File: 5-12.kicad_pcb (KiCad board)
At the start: 2 copper layers, 266.7 x 95.2 mm, 136 parts, among them SW1 SW_Push, U1 ATmega32U4-AU, Y1 16MHz

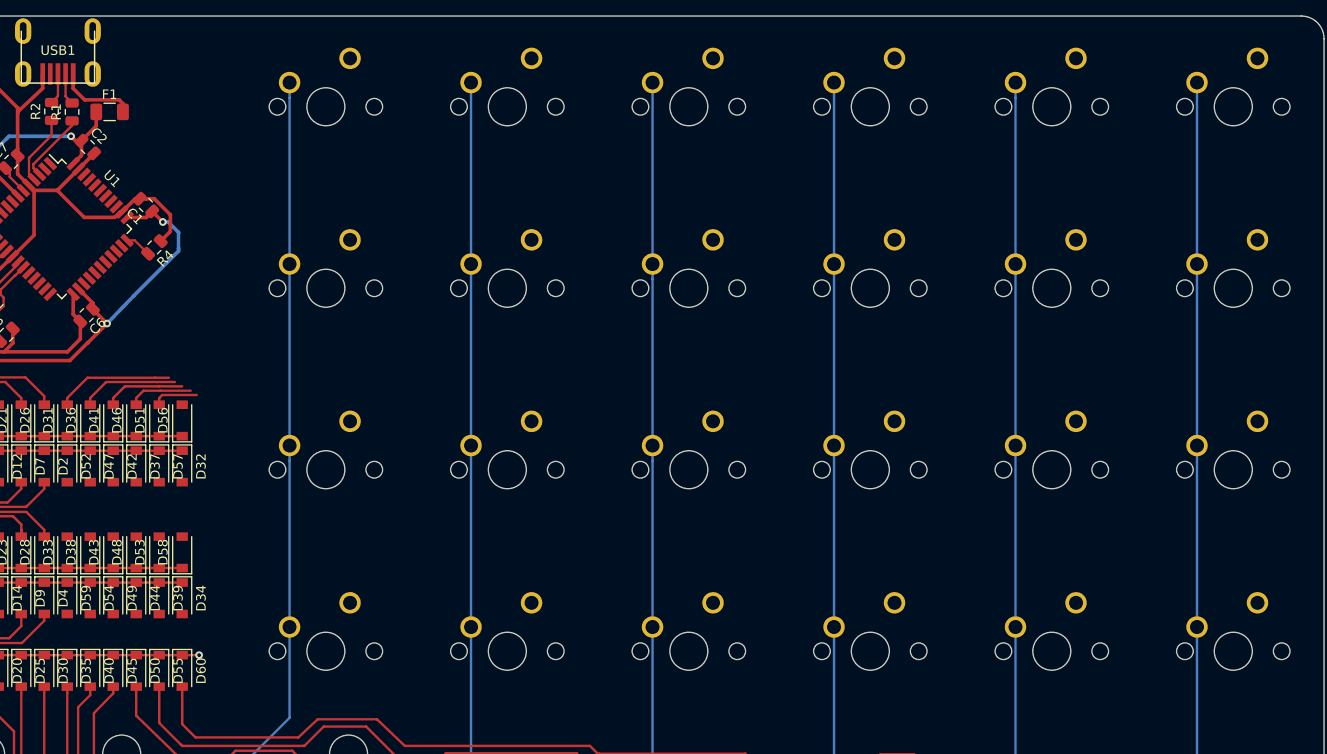
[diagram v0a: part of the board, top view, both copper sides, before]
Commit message: Finished routing switches to diode banks
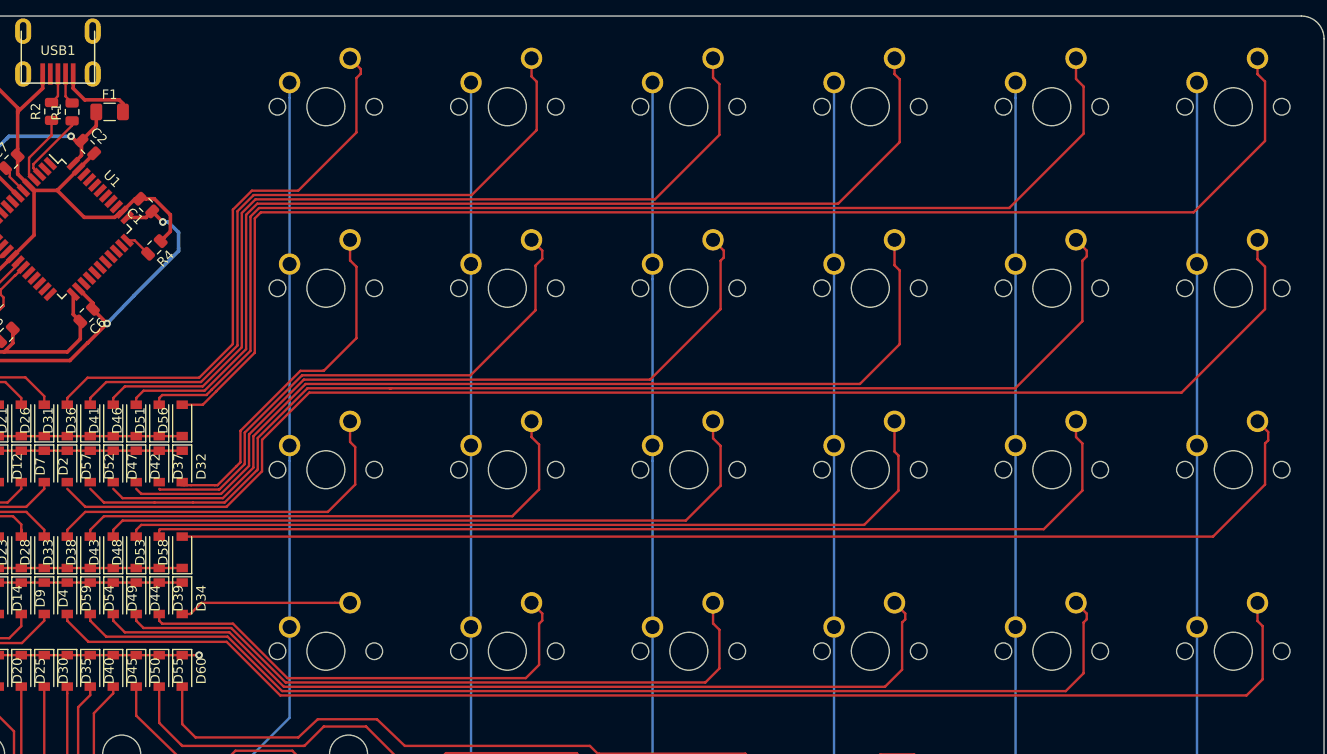
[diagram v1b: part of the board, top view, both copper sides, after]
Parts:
- moved D57 9.65 mm to (146.7, 116.3)
- moved D52 2.41 mm to (149.1, 116.3)
- moved D37 2.41 mm to (156.3, 116.3)
- moved D47 2.41 mm to (151.5, 116.3)
- moved D42 2.41 mm to (153.9, 116.3)
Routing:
- net Net-(D57-Pad2): track 0.00 -> 144.6 mm
- net Net-(D56-Pad2): track 0.00 -> 142.4 mm
- net Net-(D59-Pad2): track 0.00 -> 138.4 mm
- net Net-(D52-Pad2): track 0.00 -> 123.9 mm
- net Net-(D58-Pad2): track 0.00 -> 123.2 mm
- net Net-(D51-Pad2): track 4.77 -> 125.7 mm
- net Net-(D54-Pad2): track 0.00 -> 116.8 mm
- net Net-(D53-Pad2): track 0.00 -> 106.9 mm
- net Net-(D47-Pad2): track 0.00 -> 102.9 mm
- net Net-(D46-Pad2): track 6.74 -> 109.2 mm
- net Net-(D49-Pad2): track 0.00 -> 94.7 mm
- net Net-(D48-Pad2): track 0.00 -> 89.9 mm
- net Net-(D41-Pad2): track 8.45 -> 92.3 mm
- net Net-(D42-Pad2): track 0.00 -> 79.4 mm
- net Net-(D43-Pad2): track 0.00 -> 73.5 mm
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
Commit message: Finished pre-routing of row, col lines ahead into buses
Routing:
- net Col0: track 76.2 -> 195.8 mm
- net Col11: track 76.2 -> 188.2 mm
- net Col1: track 76.2 -> 176.6 mm
- net Col10: track 76.2 -> 169.9 mm
- net Col2: track 76.2 -> 158.2 mm
- net Col9: track 76.2 -> 153.2 mm
- net Col3: track 76.2 -> 139.4 mm
- net Col8: track 76.2 -> 135.0 mm
- net Col4: track 76.2 -> 119.6 mm
- net Col7: track 76.2 -> 114.5 mm
- net Row5: track 28.3 -> 65.2 mm
- net Row3: track 26.5 -> 57.8 mm, vias 0 -> 1
- net Row2: track 26.5 -> 55.3 mm, vias 0 -> 1
- net Col5: track 80.1 -> 104.0 mm
- net Row1: track 26.5 -> 44.2 mm, vias 0 -> 1
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
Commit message: Genned production files, made zip
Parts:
- moved C6 14.8 mm to (156.5, 87.9)
- moved C1 12.7 mm to (148.6, 99.9), turned to 225 degrees
- moved C2 8.52 mm to (140.4, 83.7), turned to 225 degrees
- moved C7 3.41 mm to (137.9, 82.5)
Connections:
- D10 pad 1: Row5 -> Row4
- D15 pad 1: Row5 -> Row4
- D20 pad 1: Row5 -> Row4
- D25 pad 1: Row5 -> Row4
- D30 pad 1: Row5 -> Row4
- D35 pad 1: Row5 -> Row4
- D40 pad 1: Row5 -> Row4
- D45 pad 1: Row5 -> Row4
- D5 pad 1: Row5 -> Row4
- D50 pad 1: Row5 -> Row4
- D55 pad 1: Row5 -> Row4
- D60 pad 1: Row5 -> Row4
- U1 pad 10: Net-(U1-Pad10) -> Col2
- U1 pad 11: Net-(U1-Pad11) -> Col3
- U1 pad 12: Net-(U1-Pad12) -> Col4
- U1 pad 18: Net-(U1-Pad18) -> Col5
- U1 pad 25: Net-(U1-Pad25) -> Row0
- U1 pad 26: Net-(U1-Pad26) -> Row1
- U1 pad 27: Net-(U1-Pad27) -> Row2
- U1 pad 28: Net-(U1-Pad28) -> Row3
- U1 pad 29: Net-(U1-Pad29) -> Row4
- U1 pad 36: Net-(U1-Pad36) -> Col6
- U1 pad 37: Net-(U1-Pad37) -> Col7
- U1 pad 38: Net-(U1-Pad38) -> Col8
- U1 pad 39: Net-(U1-Pad39) -> Col9
- U1 pad 40: Net-(U1-Pad40) -> Col10
- U1 pad 41: Net-(U1-Pad41) -> Col11
- U1 pad 8: Net-(U1-Pad8) -> Col0
- U1 pad 9: Net-(U1-Pad9) -> Col1
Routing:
- net Row4: track 0.00 -> 78.5 mm, vias 0 -> 2
- net Row5: track 65.2 -> 0.00 mm, vias 1 -> 0
- net Col5: track 104.0 -> 142.5 mm, vias 0 -> 1
- net +5V: track 104.8 -> 132.7 mm, vias 5 -> 11
- net Col0: track 195.8 -> 212.7 mm, vias 0 -> 1
- net Net-(USB1-Pad6): track 0.00 -> 16.3 mm
- net Col1: track 176.6 -> 192.7 mm, vias 0 -> 1
- net Col3: track 139.4 -> 155.2 mm, vias 0 -> 1
- net Col2: track 158.2 -> 172.9 mm, vias 0 -> 1
- net Col4: track 119.6 -> 133.1 mm, vias 0 -> 3
- net Col11: track 188.2 -> 201.5 mm, vias 0 -> 1
- net Col10: track 169.9 -> 182.0 mm, vias 0 -> 1
- net Row3: track 57.8 -> 69.9 mm, vias 1 -> 2
- net Row2: track 55.3 -> 66.4 mm, vias 1 -> 2
- net Col9: track 153.2 -> 162.4 mm, vias 0 -> 1
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- added copper zone on F.Cu, net GND
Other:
- board text added: "/u/Gigaflop"
- board text added: "GRIDLOCK"
- board text added: "woooo copper text"
